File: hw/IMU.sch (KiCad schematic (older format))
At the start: 5 parts, among them U2 LSM9DS1TR

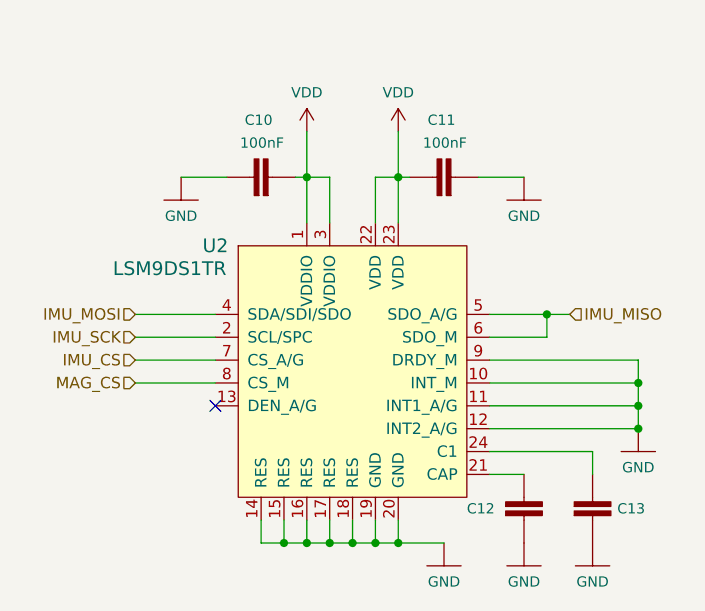
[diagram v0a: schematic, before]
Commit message: Add valid footprints to most schematic symbols. Add pin headers.
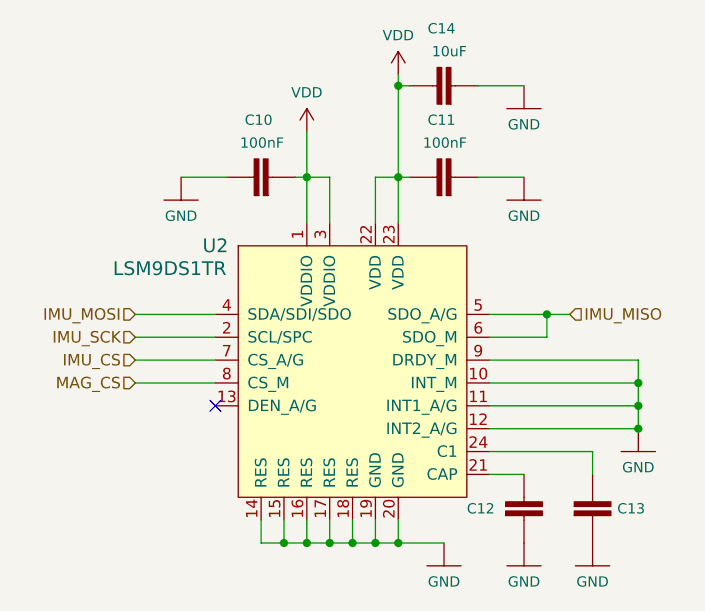
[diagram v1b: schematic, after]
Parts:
- added C14: 10uF, Capacitor_SMD:C_0603_1608Metric, symbol SparkFun-Capacitors:0.1UF-0603-25V-_+80_-20%_
- C10, C11, C12, C13: footprint 0603 -> Capacitor_SMD:C_0603_1608Metric
- U2: footprint digikey-footprints:LGA-24_3x3.5mm_LSM9DS1 -> Package_LGA:LGA-24L_3x3.5mm_P0.43mm
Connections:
- net GND: now also C14.2
- net VDD: now also C14.1
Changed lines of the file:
@@
 F 0 "U2" H 5400 4700 60  0000 C CNN
 F 1 "LSM9DS1TR" H 5200 4600 60  0000 C CNN
-F 2 "digikey-footprints:LGA-24_3x3.5mm_LSM9DS1" H 6200 4200 60  0001 L CNN
+F 2 "Package_LGA:LGA-24L_3x3.5mm_P0.43mm" H 6200 4200 60  0001 L CNN
 F 3 "http://www.st.com/content/ccc/resource/technical/document/datasheet/1e/3f/2a/d6/25/eb/48/46/DM00103319.pdf/files/DM00103319.pdf/jcr:content/translations/en.DM00103319.pdf" H 6200 4300 60  0001 L CNN
 F 4 "497-14946-1-ND" H 6200 4400 60  0001 L CNN "Digi-Key_PN"
@@
 F 0 "C12" H 6500 4550 45  0000 L CNN
 F 1 "10nF" H 6858 4508 45  0001 L CNN
-F 2 "0603" H 6750 4750 20  0001 C CNN
+F 2 "Capacitor_SMD:C_0603_1608Metric" H 6750 4750 20  0001 C CNN
 F 3 "" H 6750 4500 50  0001 C CNN
 F 4 "" H 6858 4466 60  0001 L CNN "Field4"
@@
 F 0 "C13" H 7158 4550 45  0000 L CNN
 F 1 "100nF" H 7158 4508 45  0001 L CNN
-F 2 "0603" H 7050 4750 20  0001 C CNN
+F 2 "Capacitor_SMD:C_0603_1608Metric" H 7050 4750 20  0001 C CNN
 F 3 "" H 7050 4500 50  0001 C CNN
 F 4 "" H 7158 4466 60  0001 L CNN "Field4"
@@
 L SparkFun-PowerSymbols:VDD #SUPPLY0103
 U 1 1 5DB4803D
-P 6200 2800
-F 0 "#SUPPLY0103" H 6250 2800 45  0001 L BNN
-F 1 "VDD" H 6200 2970 45  0000 C CNN
-F 2 "XXX-00000" H 6200 2981 60  0001 C CNN
-F 3 "" H 6200 2800 60  0001 C CNN
-	1    6200 2800
+P 6200 2550
+F 0 "#SUPPLY0103" H 6250 2550 45  0001 L BNN
+F 1 "VDD" H 6200 2720 45  0000 C CNN
+F 2 "XXX-00000" H 6200 2731 60  0001 C CNN
+F 3 "" H 6200 2550 60  0001 C CNN
+	1    6200 2550
 	1    0    0    -1
 $EndComp
@@
 F 0 "C10" V 5900 3000 45  0000 L CNN
 F 1 "100nF" V 5800 2950 45  0000 L CNN
-F 2 "0603" H 5650 3250 20  0001 C CNN
+F 2 "Capacitor_SMD:C_0603_1608Metric" H 5650 3250 20  0001 C CNN
 F 3 "" H 5650 3000 50  0001 C CNN
 F 4 "" H 5758 2966 60  0001 L CNN "Field4"
@@
 	5900 3000 5800 3000
 Wire Wire Line
-	6200 2800 6200 3000
-Wire Wire Line
 	6200 3000 6100 3000
 Wire Wire Line
@@
 F 0 "C11" V 6700 3000 45  0000 L CNN
 F 1 "100nF" V 6600 2950 45  0000 L CNN
-F 2 "0603" H 6450 3250 20  0001 C CNN
+F 2 "Capacitor_SMD:C_0603_1608Metric" H 6450 3250 20  0001 C CNN
 F 3 "" H 6450 3000 50  0001 C CNN
 F 4 "" H 6558 2966 60  0001 L CNN "Field4"
@@
 	0    -1   -1   0
 $EndComp
+Wire Wire Line
+	6200 2550 6200 2600
+$Comp
+L SparkFun-PowerSymbols:GND #GND0117
+U 1 1 5DBB7158
+P 6750 2600
+F 0 "#GND0117" H 6800 2550 45  0001 L BNN
+F 1 "GND" H 6750 2430 45  0000 C CNN
+F 2 "" H 6750 2500 60  0001 C CNN
+F 3 "" H 6750 2500 60  0001 C CNN
+	1    6750 2600
+	1    0    0    -1
+$EndComp
+Wire Wire Line
+	6550 2600 6750 2600
+$Comp
+L SparkFun-Capacitors:0.1UF-0603-25V-_+80_-20%_ C14
+U 1 1 5DBB7160
+P 6450 2600
+F 0 "C14" V 6700 2600 45  0000 L CNN
+F 1 "10uF" V 6600 2550 45  0000 L CNN
+F 2 "Capacitor_SMD:C_0603_1608Metric" H 6450 2850 20  0001 C CNN
+F 3 "" H 6450 2600 50  0001 C CNN
+F 4 "" H 6558 2566 60  0001 L CNN "Field4"
+	1    6450 2600
+	0    -1   -1   0
+$EndComp
+Wire Wire Line
+	6250 2600 6200 2600
+Connection ~ 6200 2600
+Wire Wire Line
+	6200 2600 6200 3000
 $EndSCHEMATC
